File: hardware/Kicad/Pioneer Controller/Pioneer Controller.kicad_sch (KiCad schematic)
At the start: 35 parts, among them J1 Sensor Connector, J2 Power (USBC), J3 Arduino-NANO-33, U1 ESP32-S3, U2 2821, U3 DS3231_Precision_RTC, U4 RFM95W_LoRa_Radio_Transceiver, U5 BME280_Temperature_Sensor

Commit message: finished first PCB draft
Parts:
- added J4: Conn_Coaxial, Connector_Coaxial:SMA_Amphenol_132134-11_Vertical, symbol Connector:Conn_Coaxial
- C1, C2, C3, C4, C5, C6, C7, C8: renamed from C?; footprint (none) -> Capacitor_SMD:C_1206_3216Metric
- D1, D2, D3: renamed from D?; footprint (none) -> LED_SMD:LED_1206_3216Metric
- L1, L2: renamed from L?; value INDUCTOR -> INDUCTOR 4.7uH; footprint (none) -> Inductor_SMD:L_1206_3216Metric
- R1, R2, R3, R4, R5, R6, R7: renamed from R?; footprint (none) -> Resistor_SMD:R_1206_3216Metric
- SW1, SW2, SW3, SW4: renamed from SW?; footprint (none) -> Button_Switch_THT:SW_PUSH_6mm
- U4: footprint Adafruit_Sensors:FM95W LoRa Radio Transceiver -> (none)
- U5: footprint Connector_PinHeader_2.54mm:PinHeader_1x04_P2.54mm_Vertical -> Adafruit_Sensors:BME280 I2C Temperature Sensor
- gave numbers to parts that had none: 2
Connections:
- net GND: now also J4.2 (Ext)
- new net SMA: J4.1 (In), U4.SMA

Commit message: stuff
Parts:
- added SW5: SW_DIP_x02, Button_Switch_THT:SW_DIP_SPSTx02_Slide_9.78x7.26mm_W7.62mm_P2.54mm, symbol Switch:SW_DIP_x02
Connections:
- net +3V3: now also SW5.3, SW5.4
- net SW6: now reaches A1.38 (GPIO20)
- net SW6: now also J3.7, U1.A5, SW5.2
- net SW5: now reaches A1.40 (GPIO21)
- net SW5: now also J3.6, U1.A4, SW5.1
- no-connect marks 60 -> 54
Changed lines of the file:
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@@
   (junction (at 24.13 91.44) (diameter 0) (color 0 0 0 0)
+  )
+  (junction (at 234.95 133.35) (diameter 0) (color 0 0 0 0)
   )
   (junction (at 17.78 161.29) (diameter 0) (color 0 0 0 0)
@@
   (no_connect (at 87.63 114.3))
   (no_connect (at 87.63 99.06))
-  (no_connect (at 87.63 101.6))
   (no_connect (at 87.63 96.52))
   (no_connect (at 87.63 116.84))
   (no_connect (at 87.63 119.38))
-  (no_connect (at 87.63 104.14))
   (no_connect (at 113.03 116.84))
   (no_connect (at 113.03 114.3))
-  (no_connect (at 87.63 106.68))
   (no_connect (at 87.63 121.92))
   (no_connect (at 113.03 121.92))
@@
   (no_connect (at 158.75 74.93))
   (no_connect (at 269.24 77.47))
-  (no_connect (at 24.13 111.76))
   (no_connect (at 24.13 104.14))
   (no_connect (at 24.13 106.68))
-  (no_connect (at 24.13 109.22))
   (no_connect (at 24.13 127))
   (no_connect (at 49.53 91.44))
@@
   (no_connect (at 24.13 35.56))
   (no_connect (at 69.85 40.64))
-  (no_connect (at 69.85 76.2))
   (no_connect (at 69.85 45.72))
   (no_connect (at 69.85 48.26))
-  (no_connect (at 69.85 73.66))
   (no_connect (at 86.36 30.48))
   (no_connect (at 86.36 35.56))
@@
   (no_connect (at 24.13 101.6))
   (no_connect (at 24.13 88.9))
+  (no_connect (at 87.63 101.6))
   (no_connect (at 143.51 35.56))
   (no_connect (at 143.51 33.02))
@@
     (stroke (width 0) (type default) (color 0 0 0 0))
   )
+  (wire (pts (xy 234.95 133.35) (xy 234.95 135.89))
+    (stroke (width 0) (type default) (color 0 0 0 0))
+  )
   (wire (pts (xy 71.12 38.1) (xy 69.85 38.1))
     (stroke (width 0) (type default) (color 0 0 0 0))
@@
     (stroke (width 0) (type default) (color 0 0 0 0))
   )
+  (wire (pts (xy 71.12 73.66) (xy 69.85 73.66))
+    (stroke (width 0) (type default) (color 0 0 0 0))
+  )
   (wire (pts (xy 87.63 127) (xy 82.55 127))
     (stroke (width 0) (type default) (color 0 0 0 0))
@@
     (stroke (width 0) (type default) (color 0 0 0 0))
   )
+  (wire (pts (xy 22.86 109.22) (xy 24.13 109.22))
+    (stroke (width 0) (type default) (color 0 0 0 0))
+  )
   (wire (pts (xy 121.92 180.34) (xy 121.92 171.45))
     (stroke (width 0) (type default) (color 0 0 0 0))
@@
     (stroke (width 0) (type default) (color 0 0 0 0))
   )
+  (wire (pts (xy 22.86 111.76) (xy 24.13 111.76))
+    (stroke (width 0) (type default) (color 0 0 0 0))
+  )
   (polyline (pts (xy 134.62 87.63) (xy 134.62 135.89))
     (stroke (width 0) (type default) (color 0 0 0 0))
@@
     (stroke (width 0) (type default) (color 0 0 0 0))
   )
-  (polyline (pts (xy 205.74 54.61) (xy 205.74 135.89))
+  (polyline (pts (xy 205.74 54.61) (xy 205.74 149.86))
     (stroke (width 0) (type default) (color 0 0 0 0))
   )
@@
     (stroke (width 0) (type default) (color 0 0 0 0))
   )
+  (wire (pts (xy 86.36 104.14) (xy 87.63 104.14))
+    (stroke (width 0) (type default) (color 0 0 0 0))
+  )
   (wire (pts (xy 262.89 27.94) (xy 266.7 27.94))
     (stroke (width 0) (type default) (color 0 0 0 0))
@@
     (stroke (width 0) (type default) (color 0 0 0 0))
   )
+  (wire (pts (xy 218.44 135.89) (xy 219.71 135.89))
+    (stroke (width 0) (type default) (color 0 0 0 0))
+  )
   (wire (pts (xy 86.36 91.44) (xy 87.63 91.44))
     (stroke (width 0) (type default) (color 0 0 0 0))
@@
     (stroke (width 0) (type default) (color 0 0 0 0))
   )
+  (wire (pts (xy 86.36 106.68) (xy 87.63 106.68))
+    (stroke (width 0) (type default) (color 0 0 0 0))
+  )
   (wire (pts (xy 22.86 33.02) (xy 24.13 33.02))
     (stroke (width 0) (type default) (color 0 0 0 0))
@@
     (stroke (width 0) (type default) (color 0 0 0 0))
   )
+  (wire (pts (xy 234.95 132.08) (xy 234.95 133.35))
+    (stroke (width 0) (type default) (color 0 0 0 0))
+  )
   (polyline (pts (xy 12.7 12.7) (xy 132.08 12.7))
     (stroke (width 0) (type default) (color 0 0 0 0))
@@
     (stroke (width 0) (type default) (color 0 0 0 0))
   )
-  (polyline (pts (xy 205.74 135.89) (xy 284.48 135.89))
+  (polyline (pts (xy 205.74 149.86) (xy 284.48 149.86))
     (stroke (width 0) (type default) (color 0 0 0 0))
   )
@@
     (stroke (width 0) (type default) (color 0 0 0 0))
   )
+  (wire (pts (xy 71.12 76.2) (xy 69.85 76.2))
+    (stroke (width 0) (type default) (color 0 0 0 0))
+  )
   (wire (pts (xy 17.78 48.26) (xy 17.78 27.94))
     (stroke (width 0) (type default) (color 0 0 0 0))
@@
     (stroke (width 0) (type default) (color 0 0 0 0))
   )
+  (wire (pts (xy 218.44 133.35) (xy 219.71 133.35))
+    (stroke (width 0) (type default) (color 0 0 0 0))
+  )
   (wire (pts (xy 22.86 124.46) (xy 24.13 124.46))
     (stroke (width 0) (type default) (color 0 0 0 0))
@@
     (stroke (width 0) (type default) (color 0 0 0 0))
   )
-  (polyline (pts (xy 284.48 135.89) (xy 284.48 54.61))
+  (polyline (pts (xy 284.48 149.86) (xy 284.48 54.61))
     (stroke (width 0) (type default) (color 0 0 0 0))
   )
@@
     (effects (font (size 1.27 1.27)) (justify left bottom))
   )
+  (label "SW6" (at 218.44 135.89 180)
+    (effects (font (size 1.27 1.27)) (justify right bottom))
+  )
   (label "MOSI" (at 114.3 93.98 0)
     (effects (font (size 1.27 1.27)) (justify left bottom))
@@
     (effects (font (size 1.27 1.27)) (justify left bottom))
   )
+  (label "SW6" (at 22.86 111.76 180)
+    (effects (font (size 1.27 1.27)) (justify right bottom))
+  )
   (label "LED2" (at 50.8 109.22 0)
     (effects (font (size 1.27 1.27)) (justify left bottom))
@@
     (effects (font (size 1.27 1.27)) (justify left bottom))
   )
+  (label "SW5" (at 22.86 109.22 180)
+    (effects (font (size 1.27 1.27)) (justify right bottom))
+  )
   (label "SDA" (at 22.86 30.48 180)
     (effects (font (size 1.27 1.27)) (justify right bottom))
@@
     (effects (font (size 1.27 1.27)) (justify right bottom))
   )
+  (label "SW5" (at 86.36 104.14 180)
+    (effects (font (size 1.27 1.27)) (justify right bottom))
+  )
   (label "MISO" (at 22.86 53.34 180)
     (effects (font (size 1.27 1.27)) (justify right bottom))
@@
     (effects (font (size 1.27 1.27)) (justify left bottom))
   )
+  (label "SW5" (at 71.12 76.2 0)
+    (effects (font (size 1.27 1.27)) (justify left bottom))
+  )
   (label "SDA" (at 86.36 109.22 180)
     (effects (font (size 1.27 1.27)) (justify right bottom))
@@
     (effects (font (size 1.27 1.27)) (justify right bottom))
   )
+  (label "SW6" (at 86.36 106.68 180)
+    (effects (font (size 1.27 1.27)) (justify right bottom))
+  )
   (label "SW2" (at 114.3 106.68 0)
     (effects (font (size 1.27 1.27)) (justify left bottom))
   )
   (label "LED3" (at 275.59 27.94 0)
+    (effects (font (size 1.27 1.27)) (justify left bottom))
+  )
+  (label "SW5" (at 218.44 133.35 180)
+    (effects (font (size 1.27 1.27)) (justify right bottom))
+  )
+  (label "SW6" (at 71.12 73.66 0)
     (effects (font (size 1.27 1.27)) (justify left bottom))
   )
@@
   )
   (symbol (lib_id "power:GND") (at 219.71 114.3 0) (unit 1)
-    (in_bom yes) (on_board yes) (fields_autoplaced)
+    (in_bom yes) (on_board yes)
     (property "Reference" "#PWR0127" (id 0) (at 219.71 120.65 0)
       (effects (font (size 1.27 1.27)) hide)
@@
     )
     (property "Datasheet" "http://www.apem.com/int/index.php?controller=attachment&id_attachment=1371" (id 3) (at 264.16 69.85 0)
+      (effects (font (size 1.27 1.27)) hide)
+    )
+    (pin "1")
+    (pin "2")
+    (pin "3")
+    (pin "4")
+  )
+  (symbol (lib_id "Switch:SW_DIP_x02") (at 227.33 135.89 0) (unit 1)
+    (in_bom yes) (on_board yes) (fields_autoplaced)
+    (property "Reference" "SW5" (id 0) (at 227.33 125.73 0))
+    (property "Value" "SW_DIP_x02" (id 1) (at 227.33 128.27 0))
+    (property "Footprint" "Button_Switch_THT:SW_DIP_SPSTx02_Slide_9.78x7.26mm_W7.62mm_P2.54mm" (id 2) (at 227.33 135.89 0)
+      (effects (font (size 1.27 1.27)) hide)
+    )
+    (property "Datasheet" "~" (id 3) (at 227.33 135.89 0)
       (effects (font (size 1.27 1.27)) hide)
     )
@@
     (pin "4")
     (pin "5")
+  )
+  (symbol (lib_id "power:+3.3V") (at 234.95 132.08 0) (unit 1)
+    (in_bom yes) (on_board yes) (fields_autoplaced)
+    (property "Reference" "#PWR?" (id 0) (at 234.95 135.89 0)
+      (effects (font (size 1.27 1.27)) hide)
+    )
+    (property "Value" "+3.3V" (id 1) (at 234.95 127 0))
+    (property "Footprint" "" (id 2) (at 234.95 132.08 0)
+      (effects (font (size 1.27 1.27)) hide)
+    )
+    (property "Datasheet" "" (id 3) (at 234.95 132.08 0)
+      (effects (font (size 1.27 1.27)) hide)
+    )
+    (pin "1")
   )
   (symbol (lib_id "power:+3.3V") (at 163.83 58.42 0) (unit 1)
@@
       (reference "#PWR0138") (unit 1) (value "GND") (footprint "")
     )
+    (path "/e3bf4acd-201b-42d8-975b-415f68b46808"
+      (reference "#PWR?") (unit 1) (value "+3.3V") (footprint "")
+    )
     (path "/a8c99d9c-3aea-461e-812a-7a66fd9c15d4"
       (reference "#U0101") (unit 1) (value "VIN") (footprint "")
@@
       (reference "SW4") (unit 1) (value "SW_MEC_5E") (footprint "Button_Switch_THT:SW_PUSH_6mm")
     )
+    (path "/acd3babe-7435-443d-9220-a17faeda9d25"
+      (reference "SW5") (unit 1) (value "SW_DIP_x02") (footprint "Button_Switch_THT:SW_DIP_SPSTx02_Slide_9.78x7.26mm_W7.62mm_P2.54mm")
+    )
     (path "/80a6f078-e001-40ad-98be-886850e762f4"

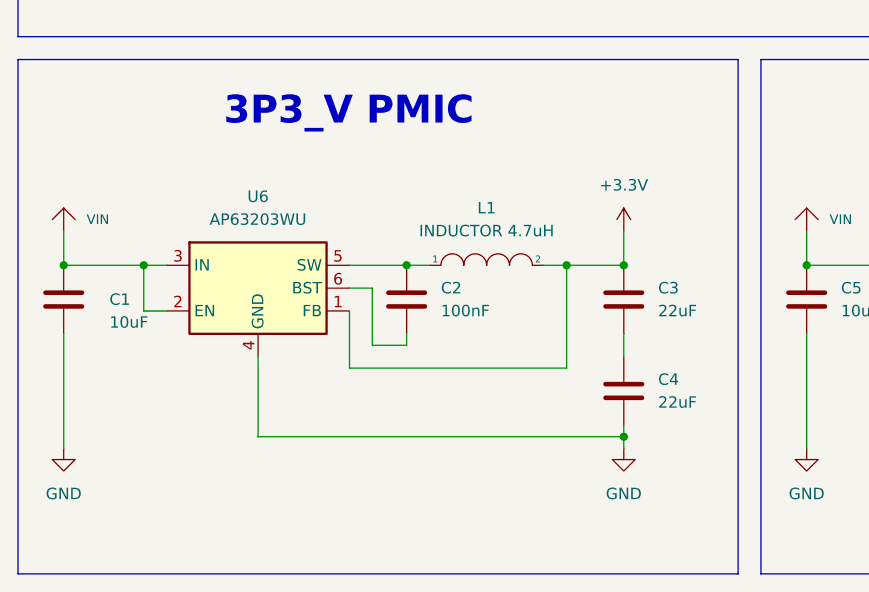
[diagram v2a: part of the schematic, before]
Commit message: updated 3.3V PMIC
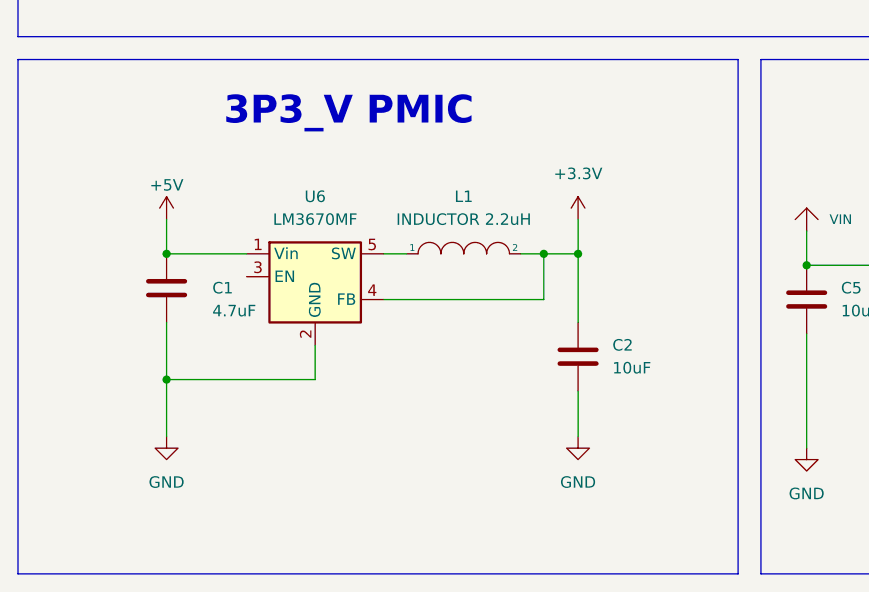
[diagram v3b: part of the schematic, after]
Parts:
- removed C3, C4: 22uF, Capacitor_SMD:C_1206_3216Metric, symbol Device:C
- removed U6: AP63203WU, Package_TO_SOT_SMD:TSOT-23-6, symbol Regulator_Switching:AP63203WU
- added U6: LM3670MF, Package_TO_SOT_SMD:TSOT-23-5, symbol Regulator_Switching:LM3670MF
- C1: value 10uF -> 4.7uF
- C2: value 100nF -> 10uF
- L1: value INDUCTOR 4.7uH -> INDUCTOR 2.2uH
- U4: footprint (none) -> Adafruit_Sensors:FM95W LoRa Radio Transceiver
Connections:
- net +3V3: now also C2.1, U6.4 (FB)
- net +5V: now also C1.1, U6.1 (Vin)
- net GND: now also C2.2, U6.2 (GND)
- net VIN: no longer C1.1
- net at L1.1: now also U6.5 (SW); no longer C2.1
